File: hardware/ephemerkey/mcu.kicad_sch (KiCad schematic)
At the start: 24 parts, among them J1 SWD TC2030-NL, J2 LOCK IF (I2C JST-PH), SW1 USER1, SW2 USER2, SW3 USER3/DFU, U1 STM32U083KCU6, Y1 32.768kHz

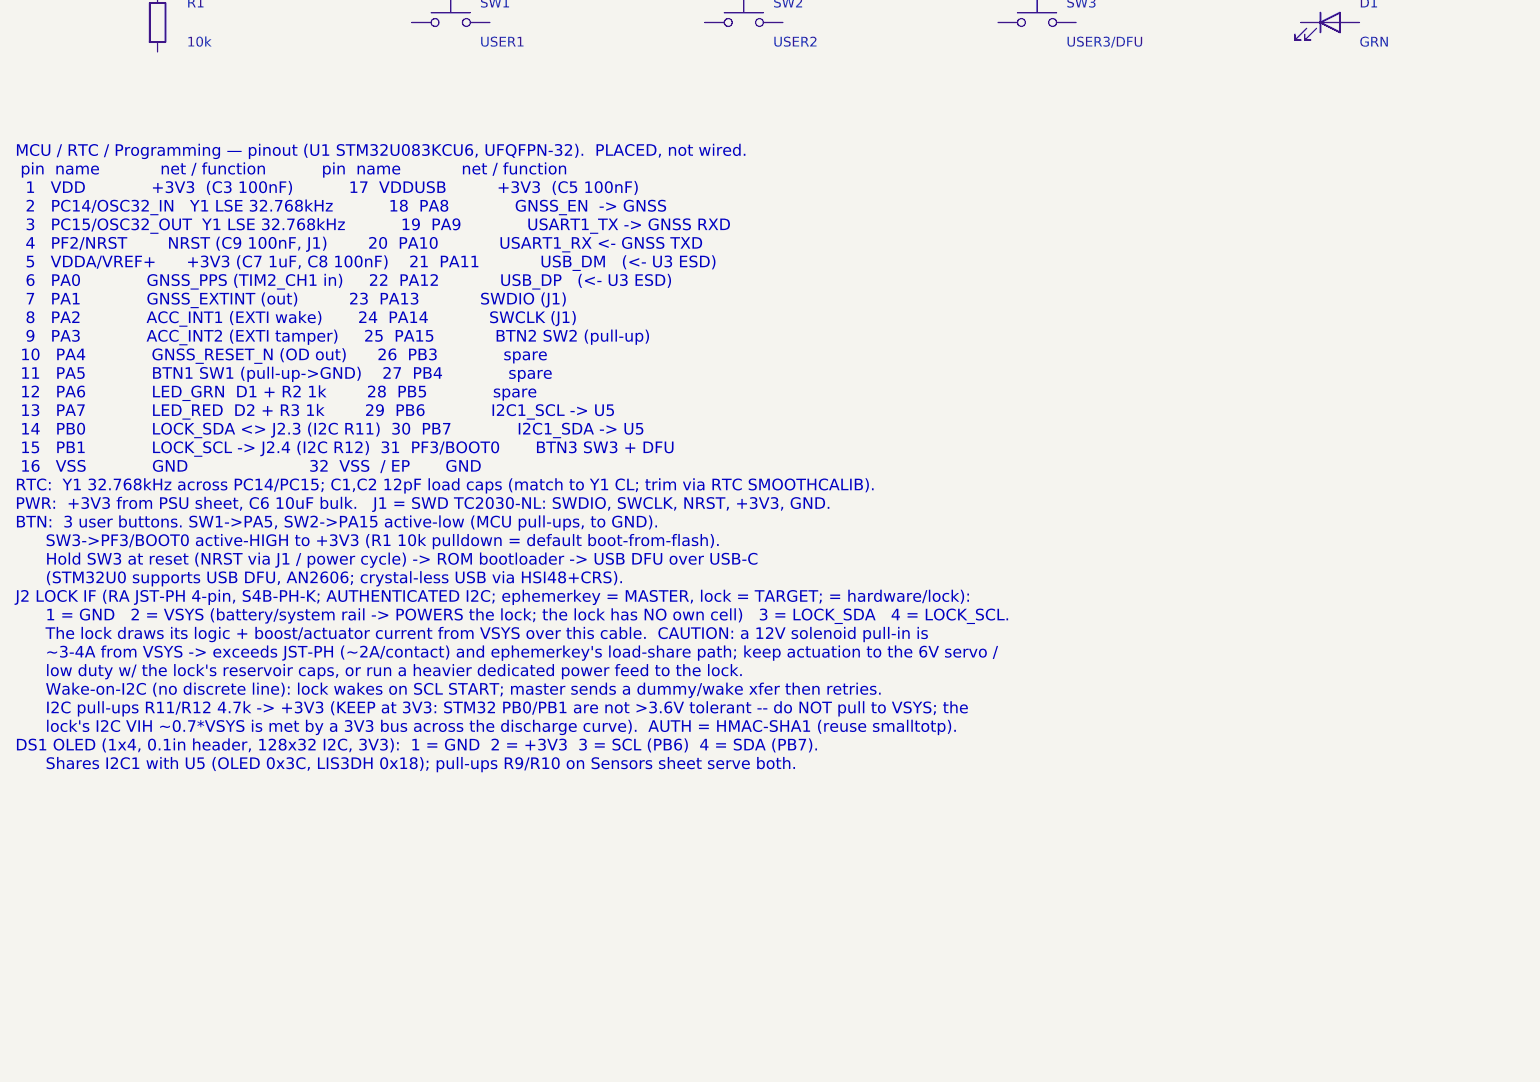
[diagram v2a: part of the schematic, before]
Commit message: ephemerkey: add buzzer (PB4/TIM3_CH1), 2nd vertical USB-C, antenna 1.8pF shunt
- Beeper: LS1 MLT-8530 (C94599, 3.6V magnetic transducer) + AO3400A low-side
  driver (Q2) + 1N4148W flyback (D5) + gate 100R/100k, driven by PB4/TIM3_CH1.
  PB4 verified as TIM3_CH1 (AF1) on the U0 family AF map; TIM3 free (PPS uses TIM2).
  Buzzer footprint is the CUI CMT-8504 placeholder -- verify vs MLT-8530 at layout.
- 2nd USB-C: J5 GCT USB4085 (C7095263), vertical, same 16-pin USB2.0 family,
  same bus as J3 (parallel VBUS/D+/D-/GND) with its own CC pulldowns R15/R16.
- Antenna: populate Cm2 = 1.8pF shunt (W3011A datasheet reference value; the -A's
  rated -16dB is measured with shunt 1.8pF), Cm3 DNP; VNA-trim at bring-up.
  MAX-M10S RF_IN has internal DC block -> no external DC-block cap. Refs: Pulse
  W3011A datasheet + u-blox MAX-M10S integration manual UBX-20053088.

Regenerated (70 components, all footprints assigned + 3D models). DESIGN.md +
per-sheet notes updated. ephemerkey was placed-not-wired, so no wiring lost.

Co-Authored-By: Claude Opus 4.8 (1M context) <noreply@anthropic.com>
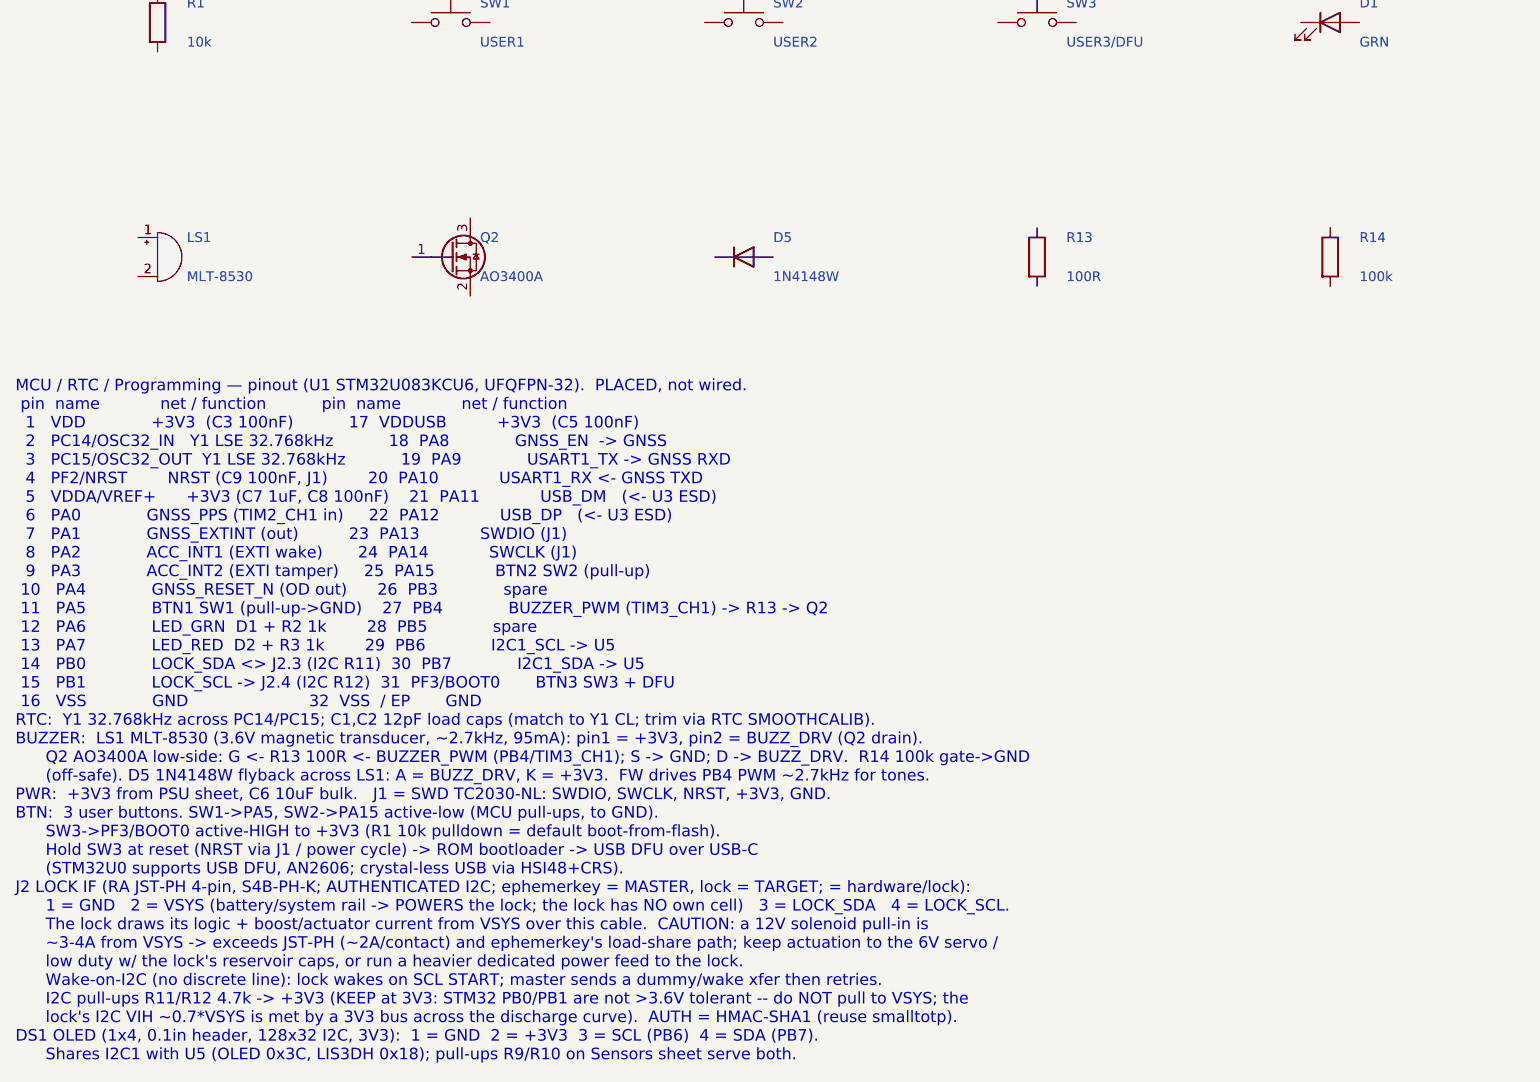
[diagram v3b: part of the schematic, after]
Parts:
- added D5: 1N4148W, Diode_SMD:D_SOD-123, symbol Device:D
- added LS1: MLT-8530, Buzzer_Beeper:MagneticBuzzer_CUI_CMT-8504-100-SMT, symbol Device:Buzzer
- added Q2: AO3400A, Package_TO_SOT_SMD:SOT-23, symbol Transistor_FET:Q_NMOS_GSD
- added R13: 100R, Resistor_SMD:R_0402_1005Metric, symbol Device:R
- added R14: 100k, Resistor_SMD:R_0402_1005Metric, symbol Device:R

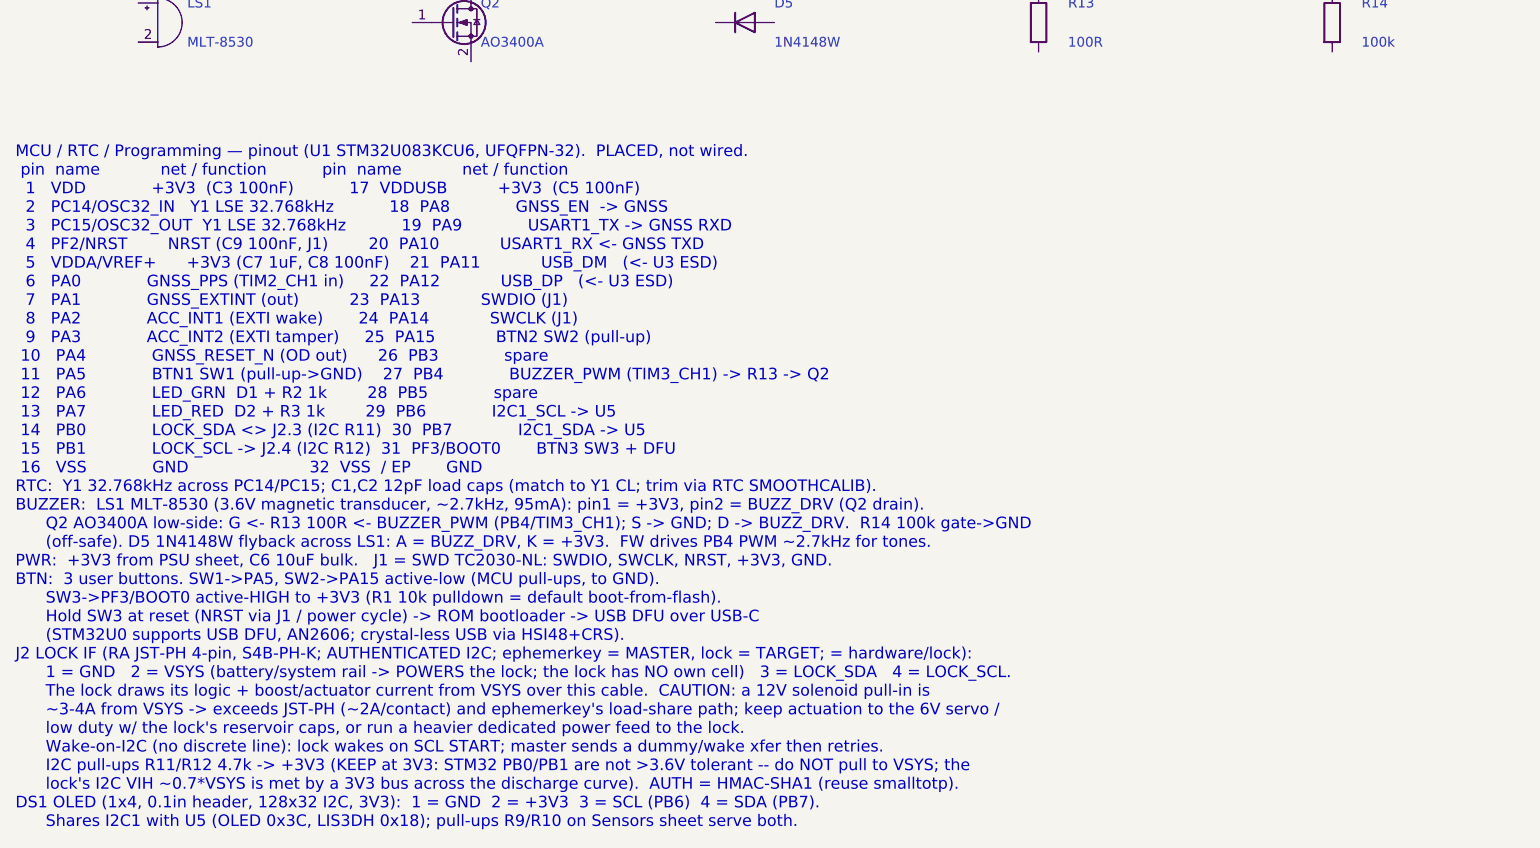
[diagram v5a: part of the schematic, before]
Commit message: hardware: fix PSU load-share S/D, make all sheet notes monospace
The PSU wiring note specified Q1 (AO3401A load-share PMOS) as S=BAT+,
D=VSYS. A PMOS body diode conducts D->S, so that orientation points the
diode VSYS -> BAT+: with USB attached VSYS sits ~4.7V (VBUS - D3) against
a 3.0-4.2V cell, forward-biasing it and dumping uncontrolled current into
the battery, bypassing the MCP73831 charger entirely.

Correct assignment is D=BAT+, S=VSYS, so the body diode points BAT+ ->
VSYS: the battery always reaches the load, and USB can never back-feed
the cell. Q1 was placed but never wired (all three pins are unconnected
in the netlist), so this is a spec fix ahead of wiring, not a board
change. The lock's Q3 is a high-side switch and deliberately uses the
opposite S/D assignment; the note now says so, to stop the two being
"reconciled" by pattern-matching.

Also relaid the PSU note as a two-column table and gave every sheet note
the Courier New face the generator already emits (kschgen NOTE_FONT, added
in 43a6067). The sheets predate that commit, so their notes rendered in
KiCad's variable-width stroke font and the space-padded pin tables did not
line up. Font only on the other six notes -- text is untouched.

Verified: kicad-cli netlists for both boards are byte-identical before and
after (ephemerkey 259 nodes, lock 131 nodes) once the export timestamp is
excluded; no non-font lines changed in any sheet; all sheets re-rendered
and the notes fit inside the page frame.

The four ephemerkey sheets also carry pre-existing eeschema reformatting
(expanded lib_symbols) that was already in the working tree.

Co-Authored-By: Claude Opus 4.8 (1M context) <noreply@anthropic.com>
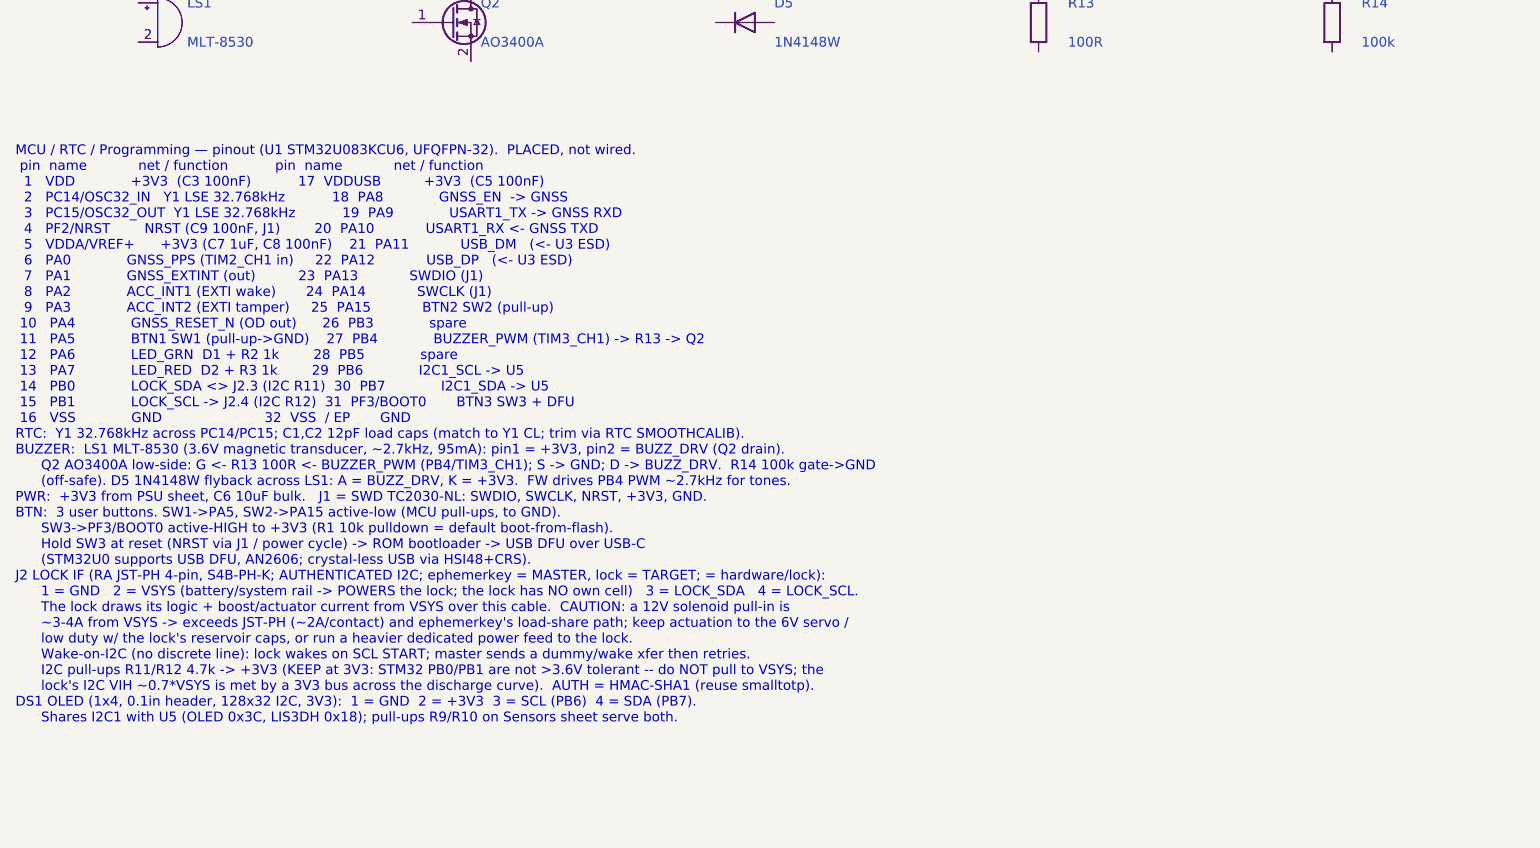
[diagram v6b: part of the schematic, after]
